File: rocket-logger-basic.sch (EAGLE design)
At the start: 57 parts, among them IC1 CC430F513X, Q2 MOSFET-PCHANNEL, U1 MAX1555, U2 MAX1555, X1 0896BM15A0001, X2 USB-MICROB, X3 SMA-142-0701-801/806

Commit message: some routing done, changed lipo charger
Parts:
- removed U1: MAX1555, SparkFun:MAX1555
- added C19: (no value), resistor:C-EUC0402
- added R13: (no value), rcl:R-EU_R0402
- added U$1: JST-ZR-2, Mine:JST-ZR-2
- added U$2: JST-ZR-2SMD, Mine:JST-ZR-2SMD
- added U3: MCP73831, SparkFun-PowerIC:MCP73831
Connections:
- new net N$1: R13.1, U3.PROG
- net +3V3: now also C19.2
- net GND: now also C19.1, R13.2, U$1.2, U$2.2, U3.VSS; no longer U1.GND
- net N$18: now also U3.VIN; no longer U1.USB
- net N$19: now also U3.STAT; no longer U1.CHG
- net N$2: now also U$1.1, U$2.1, U3.VBAT; no longer U1.BATT
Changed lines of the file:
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@@
 <layer number="106" name="bPlate" color="7" fill="1" visible="yes" active="yes"/>
 <layer number="107" name="Crop" color="7" fill="1" visible="yes" active="yes"/>
+<layer number="108" name="tplace-old" color="10" fill="1" visible="yes" active="yes"/>
+<layer number="109" name="ref-old" color="11" fill="1" visible="yes" active="yes"/>
 <layer number="116" name="Patch_BOT" color="9" fill="4" visible="yes" active="yes"/>
 <layer number="121" name="_tsilk" color="7" fill="1" visible="yes" active="yes"/>
@@
 <layer number="144" name="Drill_legend" color="7" fill="1" visible="yes" active="yes"/>
 <layer number="151" name="HeatSink" color="7" fill="1" visible="yes" active="yes"/>
+<layer number="199" name="Contour" color="7" fill="1" visible="yes" active="yes"/>
 <layer number="200" name="200bmp" color="1" fill="10" visible="yes" active="yes"/>
 <layer number="201" name="201bmp" color="2" fill="10" visible="yes" active="yes"/>
@@
 <part name="IC1" library="Mine" deviceset="CC430F513X" device=""/>
 <part name="X1" library="Mine" deviceset="0896BM15A0001" device=""/>
-<part name="U1" library="SparkFun" deviceset="MAX1555" device=""/>
 <part name="LED1" library="SparkFun" deviceset="LED" device="0603"/>
 <part name="LED2" library="SparkFun" deviceset="LED" device="0603"/>
@@
 <part name="X2" library="SparkFun" deviceset="USB" device="-MICROB"/>
 <part name="GND32" library="SparkFun" deviceset="GND" device=""/>
-<part name="GND13" library="SparkFun" deviceset="GND" device=""/>
 <part name="C11" library="resistor" deviceset="C-EU" device="C0402"/>
 <part name="GND14" library="SparkFun" deviceset="GND" device=""/>
@@
 <part name="Q2" library="SparkFun" deviceset="MOSFET-PCHANNEL" device=""/>
 <part name="R12" library="rcl" deviceset="R-EU_" device="R0402"/>
+<part name="U$1" library="Mine" deviceset="JST-ZR-2" device=""/>
+<part name="U$2" library="Mine" deviceset="JST-ZR-2" device="SMD"/>
+<part name="GND31" library="SparkFun" deviceset="GND" device=""/>
+<part name="GND33" library="SparkFun" deviceset="GND" device=""/>
+<part name="U3" library="SparkFun-PowerIC" deviceset="MCP73831" device=""/>
+<part name="R13" library="rcl" deviceset="R-EU_" device="R0402"/>
+<part name="GND34" library="SparkFun" deviceset="GND" device=""/>
+<part name="GND35" library="SparkFun" deviceset="GND" device=""/>
+<part name="C19" library="resistor" deviceset="C-EU" device="C0402"/>
+<part name="GND13" library="supply1" deviceset="GND" device=""/>
 </parts>
 <sheets>
@@
 <instance part="IC1" gate="G$1" x="53.34" y="160.02"/>
 <instance part="X1" gate="G$1" x="-29.21" y="170.18" rot="MR0"/>
-<instance part="U1" gate="G$1" x="124.46" y="226.06"/>
 <instance part="LED1" gate="G$1" x="100.33" y="149.86" rot="R90"/>
 <instance part="LED2" gate="G$1" x="100.33" y="146.05" rot="R90"/>
@@
 <instance part="X2" gate="G$1" x="96.52" y="229.87" rot="R180"/>
 <instance part="GND32" gate="1" x="100.33" y="238.76" smashed="yes" rot="R180"/>
-<instance part="GND13" gate="1" x="106.68" y="226.06" smashed="yes" rot="R270"/>
 <instance part="C11" gate="G$1" x="105.41" y="233.68" rot="MR0"/>
 <instance part="GND14" gate="1" x="105.41" y="238.76" smashed="yes" rot="R180"/>
@@
 <instance part="Q2" gate="G$1" x="137.16" y="294.64" rot="MR90"/>
 <instance part="R12" gate="G$1" x="138.43" y="267.97" rot="R270"/>
+<instance part="U$1" gate="G$1" x="160.02" y="248.92" rot="R270"/>
+<instance part="U$2" gate="G$1" x="170.18" y="248.92" rot="R270"/>
+<instance part="GND31" gate="1" x="172.72" y="238.76" smashed="yes"/>
+<instance part="GND33" gate="1" x="162.56" y="238.76" smashed="yes"/>
+<instance part="U3" gate="G$1" x="119.38" y="226.06"/>
+<instance part="R13" gate="G$1" x="132.08" y="214.63" rot="R270"/>
+<instance part="GND34" gate="1" x="135.89" y="223.52" smashed="yes" rot="R90"/>
+<instance part="GND35" gate="1" x="132.08" y="207.01" smashed="yes"/>
+<instance part="C19" gate="G$1" x="57.15" y="208.28" rot="MR0"/>
+<instance part="GND13" gate="1" x="57.15" y="213.36" rot="R180"/>
 </instances>
 <busses>
@@
 </segment>
 <segment>
-<pinref part="U1" gate="G$1" pin="GND"/>
-<pinref part="GND13" gate="1" pin="GND"/>
-</segment>
-<segment>
 <pinref part="C11" gate="G$1" pin="1"/>
 <pinref part="GND14" gate="1" pin="GND"/>
@@
 <pinref part="JP3" gate="G$1" pin="2"/>
 </segment>
+<segment>
+<pinref part="U$2" gate="G$1" pin="2"/>
+<pinref part="GND31" gate="1" pin="GND"/>
+</segment>
+<segment>
+<pinref part="U$1" gate="G$1" pin="2"/>
+<pinref part="GND33" gate="1" pin="GND"/>
+</segment>
+<segment>
+<pinref part="R13" gate="G$1" pin="2"/>
+<pinref part="GND35" gate="1" pin="GND"/>
+</segment>
+<segment>
+<pinref part="U3" gate="G$1" pin="VSS"/>
+<pinref part="GND34" gate="1" pin="GND"/>
+<wire x1="129.54" y1="223.52" x2="133.35" y2="223.52" width="0.1524" layer="91"/>
+</segment>
+<segment>
+<pinref part="C19" gate="G$1" pin="1"/>
+<pinref part="GND13" gate="1" pin="GND"/>
+</segment>
 </net>
 <net name="N$2" class="0">
 <segment>
-<pinref part="U1" gate="G$1" pin="BATT"/>
-<wire x1="137.16" y1="228.6" x2="139.7" y2="228.6" width="0.1524" layer="91"/>
 <pinref part="JP1" gate="G$1" pin="2"/>
 <wire x1="139.7" y1="228.6" x2="149.86" y2="228.6" width="0.1524" layer="91"/>
@@
 <pinref part="R8" gate="G$1" pin="1"/>
 <wire x1="139.7" y1="204.47" x2="139.7" y2="214.63" width="0.1524" layer="91"/>
+<pinref part="U$2" gate="G$1" pin="1"/>
+<wire x1="170.18" y1="241.3" x2="170.18" y2="236.22" width="0.1524" layer="91"/>
+<wire x1="170.18" y1="236.22" x2="160.02" y2="236.22" width="0.1524" layer="91"/>
+<pinref part="U$1" gate="G$1" pin="1"/>
+<wire x1="160.02" y1="236.22" x2="149.86" y2="236.22" width="0.1524" layer="91"/>
+<wire x1="160.02" y1="241.3" x2="160.02" y2="236.22" width="0.1524" layer="91"/>
+<junction x="149.86" y="236.22"/>
+<junction x="160.02" y="236.22"/>
+<pinref part="U3" gate="G$1" pin="VBAT"/>
+<wire x1="129.54" y1="228.6" x2="139.7" y2="228.6" width="0.1524" layer="91"/>
 </segment>
 </net>
@@
 <wire x1="31.75" y1="199.39" x2="33.02" y2="199.39" width="0.1524" layer="91"/>
 <junction x="33.02" y="199.39"/>
+<pinref part="C19" gate="G$1" pin="2"/>
+<wire x1="50.8" y1="200.66" x2="57.15" y2="200.66" width="0.1524" layer="91"/>
+<wire x1="57.15" y1="200.66" x2="57.15" y2="203.2" width="0.1524" layer="91"/>
+<junction x="50.8" y="200.66"/>
 </segment>
 <segment>
@@
 <wire x1="101.6" y1="227.33" x2="105.41" y2="227.33" width="0.1524" layer="91"/>
 <wire x1="105.41" y1="227.33" x2="105.41" y2="228.6" width="0.1524" layer="91"/>
-<pinref part="U1" gate="G$1" pin="USB"/>
 <wire x1="105.41" y1="228.6" x2="109.22" y2="228.6" width="0.1524" layer="91"/>
 <pinref part="C11" gate="G$1" pin="2"/>
@@
 <wire x1="101.6" y1="198.12" x2="101.6" y2="227.33" width="0.1524" layer="91"/>
 <junction x="101.6" y="227.33"/>
+<pinref part="U3" gate="G$1" pin="VIN"/>
 </segment>
 </net>
 <net name="N$19" class="0">
 <segment>
-<pinref part="U1" gate="G$1" pin="CHG"/>
 <pinref part="LED3" gate="G$1" pin="C"/>
 <wire x1="109.22" y1="223.52" x2="109.22" y2="219.71" width="0.1524" layer="91"/>
+<pinref part="U3" gate="G$1" pin="STAT"/>
 </segment>
 </net>
@@
 </segment>
 </net>
+<net name="N$1" class="0">
+<segment>
+<pinref part="U3" gate="G$1" pin="PROG"/>
+<wire x1="129.54" y1="226.06" x2="132.08" y2="226.06" width="0.1524" layer="91"/>
+<wire x1="132.08" y1="226.06" x2="132.08" y2="219.71" width="0.1524" layer="91"/>
+<pinref part="R13" gate="G$1" pin="1"/>
+</segment>
+</net>

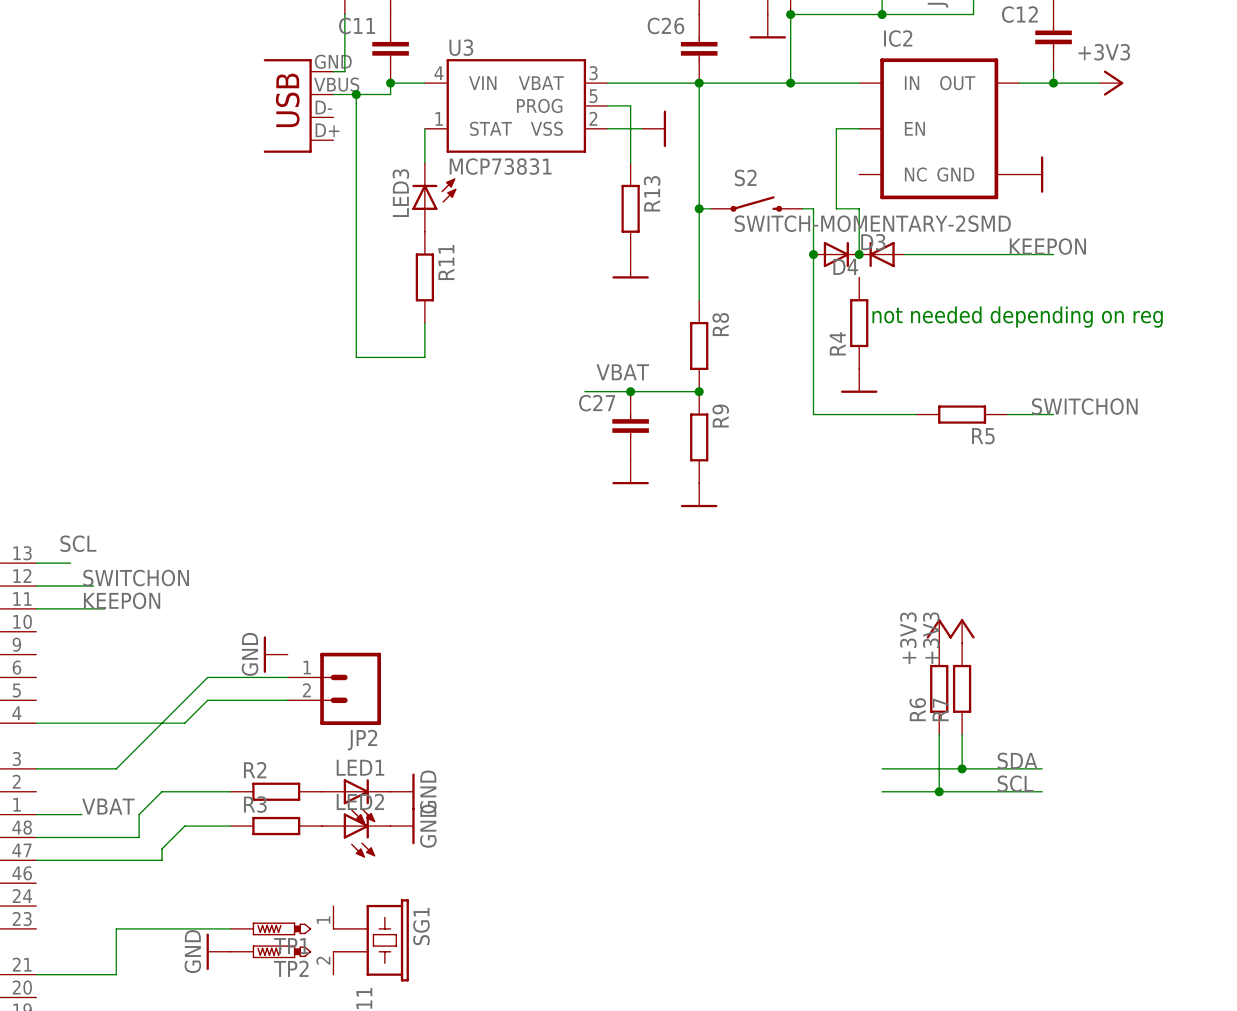
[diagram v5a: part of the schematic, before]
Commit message: moved leds and done silk layer
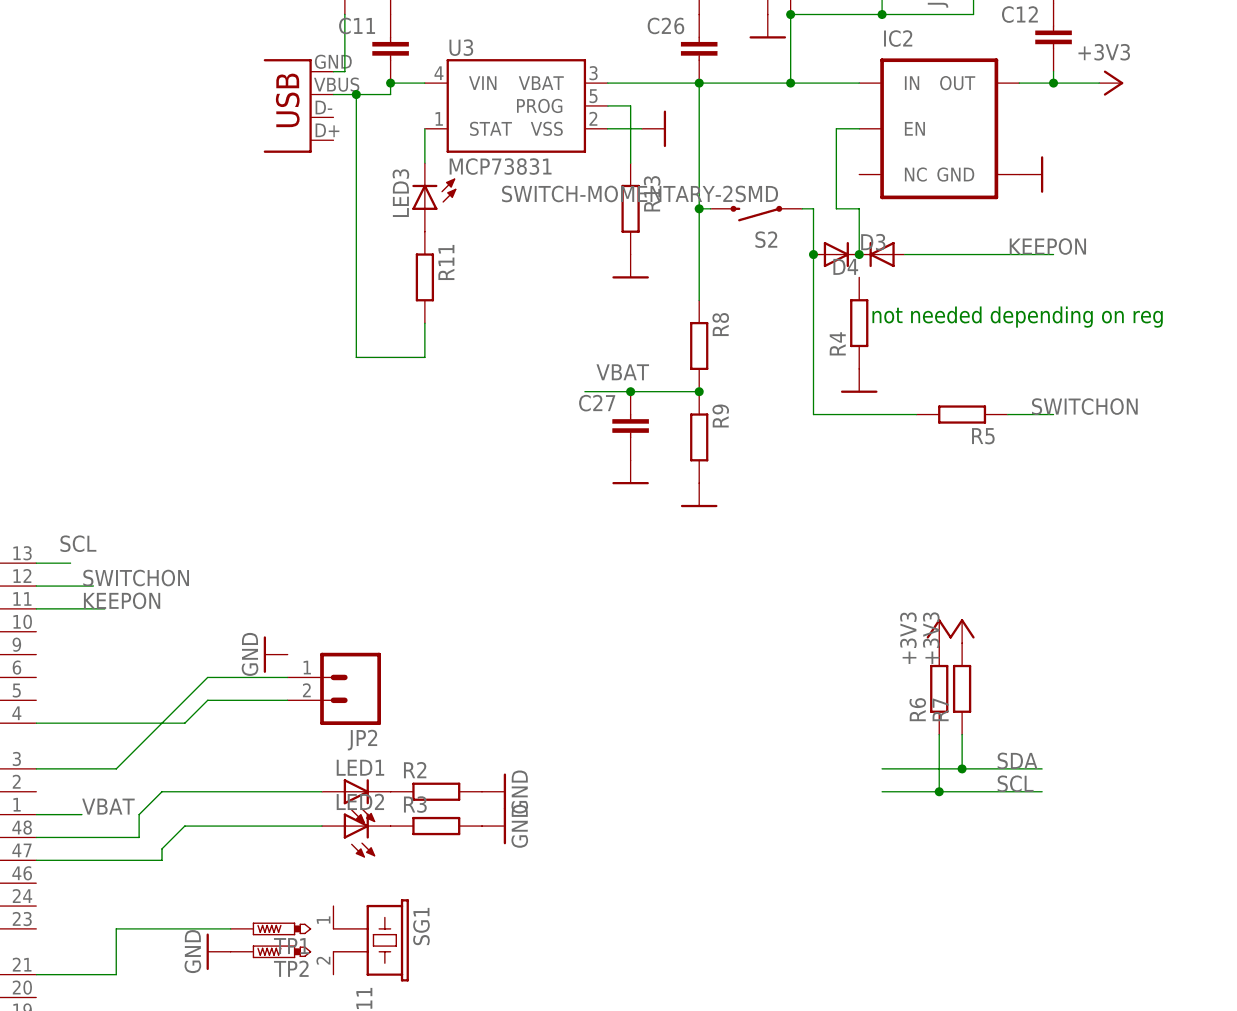
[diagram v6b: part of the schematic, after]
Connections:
- removed net N$17: IC1.P2.4, R3.1
- new net N$28: IC1.P2.4, LED2.A
- net GND: now also R2.2, R3.2; no longer LED1.C, LED2.C
- net N$10: now also LED2.C, R3.1; no longer LED2.A, R3.2
- net N$16: now also LED1.A; no longer R2.1
- net N$2: now also S2.2; no longer S2.1
- net N$24: now also S2.1; no longer S2.2
- net N$9: now also LED1.C, R2.1; no longer LED1.A, R2.2
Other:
- moved on the sheet: R2, R3, S2
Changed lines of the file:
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@@
 <instance part="X3" gate="G1" x="-49.53" y="172.72"/>
 <instance part="GND22" gate="1" x="-46.99" y="167.64"/>
-<instance part="R2" gate="G$1" x="92.71" y="149.86"/>
-<instance part="R3" gate="G$1" x="92.71" y="146.05"/>
+<instance part="R2" gate="G$1" x="110.49" y="149.86"/>
+<instance part="R3" gate="G$1" x="110.49" y="146.05"/>
 <instance part="C15" gate="G$1" x="231.14" y="182.88" rot="MR270"/>
 <instance part="C16" gate="G$1" x="227.33" y="187.96" rot="MR270"/>
@@
 <instance part="+3V4" gate="G$1" x="237.49" y="195.58"/>
 <instance part="+3V5" gate="G$1" x="242.57" y="195.58"/>
-<instance part="S2" gate="G$1" x="146.05" y="214.63"/>
+<instance part="S2" gate="G$1" x="146.05" y="214.63" rot="R180"/>
 <instance part="GND44" gate="1" x="91.44" y="165.1" rot="R270"/>
 <instance part="JP2" gate="G$1" x="101.6" y="162.56" rot="R180"/>
@@
 <instance part="C26" gate="G$1" x="139.7" y="233.68" rot="MR0"/>
 <instance part="GND46" gate="1" x="139.7" y="238.76" smashed="yes" rot="R180"/>
-<instance part="GND23" gate="1" x="107.95" y="149.86" rot="R90"/>
-<instance part="GND24" gate="1" x="107.95" y="146.05" rot="R90"/>
+<instance part="GND23" gate="1" x="118.11" y="149.86" rot="R90"/>
+<instance part="GND24" gate="1" x="118.11" y="146.05" rot="R90"/>
 <instance part="L1" gate="G$1" x="26.67" y="196.85"/>
 <instance part="TP1" gate="G$1" x="90.17" y="134.62" rot="R90"/>
@@
 </segment>
 <segment>
-<pinref part="LED1" gate="G$1" pin="C"/>
-<pinref part="GND23" gate="1" pin="GND"/>
-</segment>
-<segment>
-<pinref part="LED2" gate="G$1" pin="C"/>
-<pinref part="GND24" gate="1" pin="GND"/>
-</segment>
-<segment>
 <pinref part="TP2" gate="G$1" pin="TP"/>
 <pinref part="GND47" gate="1" pin="GND"/>
@@
 <pinref part="C19" gate="G$1" pin="1"/>
 <pinref part="GND13" gate="1" pin="GND"/>
+</segment>
+<segment>
+<pinref part="R2" gate="G$1" pin="2"/>
+<pinref part="GND23" gate="1" pin="GND"/>
+</segment>
+<segment>
+<pinref part="R3" gate="G$1" pin="2"/>
+<pinref part="GND24" gate="1" pin="GND"/>
 </segment>
 </net>
@@
 <pinref part="IC2" gate="G$1" pin="IN"/>
 <junction x="139.7" y="228.6"/>
-<pinref part="S2" gate="G$1" pin="1"/>
-<wire x1="139.7" y1="214.63" x2="139.7" y2="228.6" width="0.1524" layer="91"/>
-<wire x1="140.97" y1="214.63" x2="139.7" y2="214.63" width="0.1524" layer="91"/>
-<junction x="139.7" y="214.63"/>
+<wire x1="139.7" y1="204.47" x2="139.7" y2="214.63" width="0.1524" layer="91"/>
 <pinref part="C26" gate="G$1" pin="2"/>
 <pinref part="R8" gate="G$1" pin="1"/>
-<wire x1="139.7" y1="204.47" x2="139.7" y2="214.63" width="0.1524" layer="91"/>
 <pinref part="U$2" gate="G$1" pin="1"/>
+<wire x1="139.7" y1="214.63" x2="139.7" y2="228.6" width="0.1524" layer="91"/>
 <wire x1="170.18" y1="241.3" x2="170.18" y2="236.22" width="0.1524" layer="91"/>
 <wire x1="170.18" y1="236.22" x2="160.02" y2="236.22" width="0.1524" layer="91"/>
@@
 <pinref part="U3" gate="G$1" pin="VBAT"/>
 <wire x1="129.54" y1="228.6" x2="139.7" y2="228.6" width="0.1524" layer="91"/>
+<pinref part="S2" gate="G$1" pin="2"/>
+<wire x1="140.97" y1="214.63" x2="139.7" y2="214.63" width="0.1524" layer="91"/>
+<junction x="139.7" y="214.63"/>
 </segment>
 </net>
@@
 <segment>
 <wire x1="80.01" y1="149.86" x2="77.47" y2="147.32" width="0.1524" layer="91"/>
-<wire x1="80.01" y1="149.86" x2="87.63" y2="149.86" width="0.1524" layer="91"/>
-<pinref part="R2" gate="G$1" pin="1"/>
 <pinref part="IC1" gate="G$1" pin="P2.3"/>
 <wire x1="66.04" y1="144.78" x2="77.47" y2="144.78" width="0.1524" layer="91"/>
 <wire x1="77.47" y1="144.78" x2="77.47" y2="147.32" width="0.1524" layer="91"/>
-</segment>
-</net>
-<net name="N$17" class="0">
-<segment>
-<pinref part="R3" gate="G$1" pin="1"/>
-<wire x1="87.63" y1="146.05" x2="82.55" y2="146.05" width="0.1524" layer="91"/>
-<wire x1="82.55" y1="146.05" x2="80.01" y2="143.51" width="0.1524" layer="91"/>
-<pinref part="IC1" gate="G$1" pin="P2.4"/>
-<wire x1="66.04" y1="142.24" x2="80.01" y2="142.24" width="0.1524" layer="91"/>
-<wire x1="80.01" y1="142.24" x2="80.01" y2="143.51" width="0.1524" layer="91"/>
+<pinref part="LED1" gate="G$1" pin="A"/>
+<wire x1="97.79" y1="149.86" x2="80.01" y2="149.86" width="0.1524" layer="91"/>
 </segment>
 </net>
@@
 <segment>
 <pinref part="D3" gate="G$1" pin="A"/>
-<pinref part="S2" gate="G$1" pin="2"/>
-<wire x1="151.13" y1="214.63" x2="152.4" y2="214.63" width="0.1524" layer="91"/>
 <wire x1="152.4" y1="214.63" x2="152.4" y2="209.55" width="0.1524" layer="91"/>
 <junction x="152.4" y="209.55"/>
@@
 <wire x1="152.4" y1="191.77" x2="163.83" y2="191.77" width="0.1524" layer="91"/>
 <pinref part="R5" gate="G$1" pin="2"/>
+<pinref part="S2" gate="G$1" pin="1"/>
+<wire x1="151.13" y1="214.63" x2="152.4" y2="214.63" width="0.1524" layer="91"/>
 </segment>
 </net>
@@
 <wire x1="-11.43" y1="115.57" x2="-11.43" y2="120.65" width="0.1524" layer="91"/>
 <pinref part="JP3" gate="G$1" pin="3"/>
-</segment>
-</net>
-<net name="N$9" class="0">
-<segment>
-<pinref part="R2" gate="G$1" pin="2"/>
-<pinref part="LED1" gate="G$1" pin="A"/>
-</segment>
-</net>
-<net name="N$10" class="0">
-<segment>
-<pinref part="R3" gate="G$1" pin="2"/>
-<pinref part="LED2" gate="G$1" pin="A"/>
 </segment>
 </net>
@@
 </segment>
 </net>
+<net name="N$9" class="0">
+<segment>
+<pinref part="LED1" gate="G$1" pin="C"/>
+<pinref part="R2" gate="G$1" pin="1"/>
+</segment>
+</net>
+<net name="N$10" class="0">
+<segment>
+<pinref part="LED2" gate="G$1" pin="C"/>
+<pinref part="R3" gate="G$1" pin="1"/>
+</segment>
+</net>
+<net name="N$28" class="0">
+<segment>
+<pinref part="LED2" gate="G$1" pin="A"/>
+<wire x1="82.55" y1="146.05" x2="80.01" y2="143.51" width="0.1524" layer="91"/>
+<pinref part="IC1" gate="G$1" pin="P2.4"/>
+<wire x1="66.04" y1="142.24" x2="80.01" y2="142.24" width="0.1524" layer="91"/>
+<wire x1="80.01" y1="142.24" x2="80.01" y2="143.51" width="0.1524" layer="91"/>
+<wire x1="97.79" y1="146.05" x2="82.55" y2="146.05" width="0.1524" layer="91"/>
+</segment>
+</net>
